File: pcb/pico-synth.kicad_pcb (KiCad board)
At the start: 2 copper layers, 55.8 x 82.8 mm, 49 parts, among them J1 JST XH 2P, J2 JST XH 5P, J3 JST XH 4P, J4 JST XH 3P, SW1 Rotary_Encoder_Switch, U1 Pico, U2 6N137, U3 24LC512, U4 MCP4822, U5 LTC1044, U6 TL071, U7 TL072

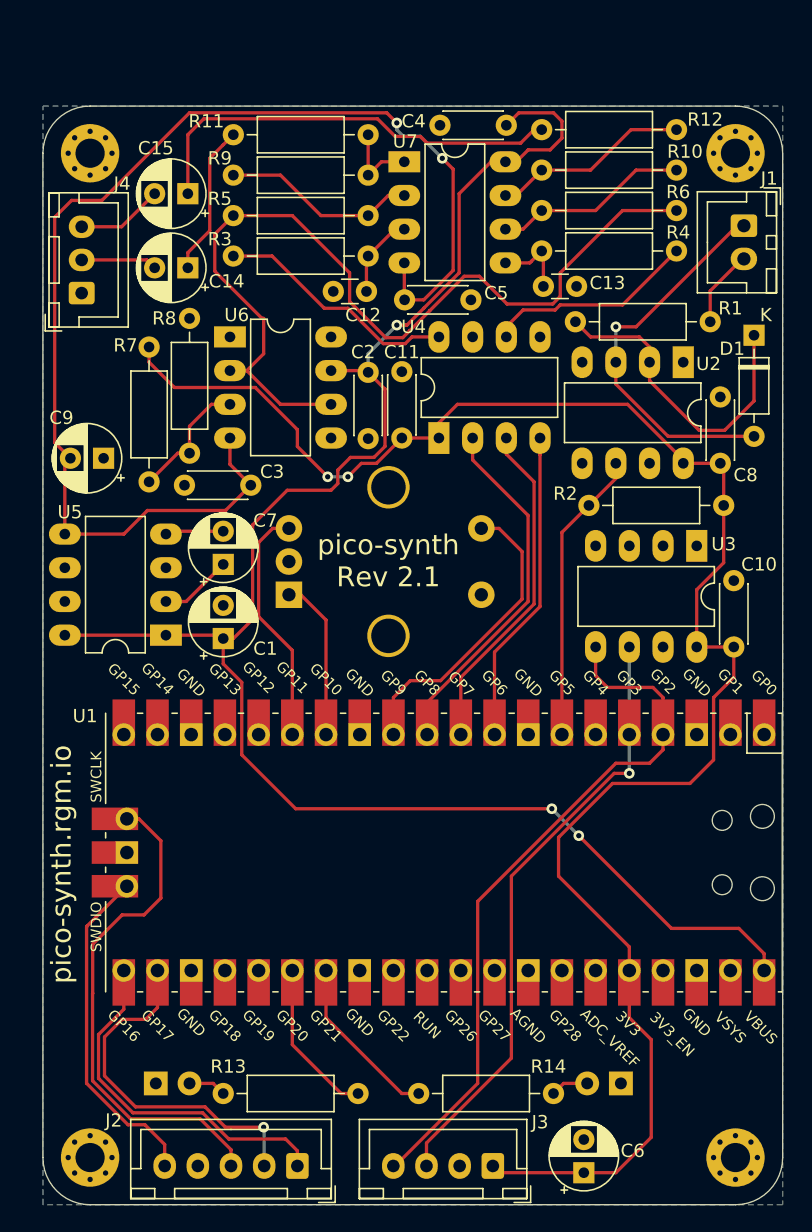
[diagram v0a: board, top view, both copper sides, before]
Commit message: pcb: upgrade to kicad 6
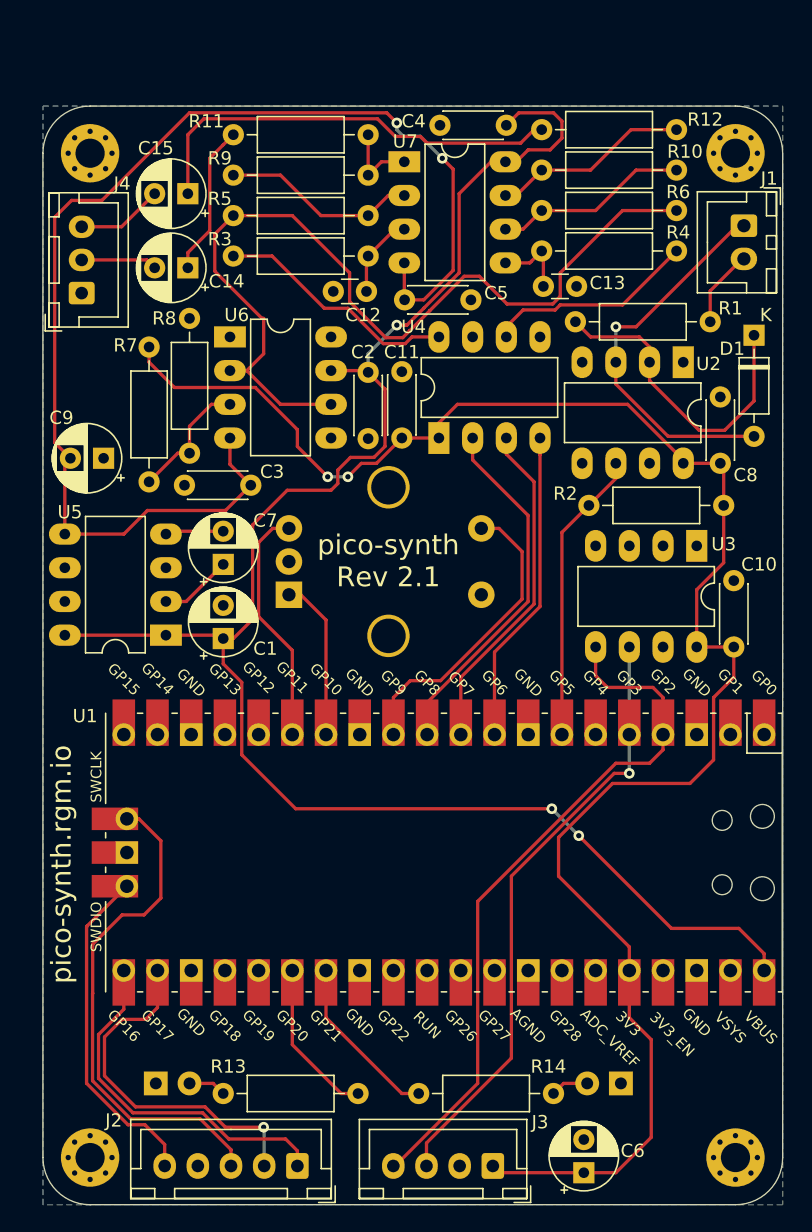
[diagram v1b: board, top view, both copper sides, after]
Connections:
- U1 pad 1: Net-(U1-Pad1) -> unconnected-(U1-Pad1)
- U1 pad 16: Net-(U1-Pad16) -> unconnected-(U1-Pad16)
- U1 pad 17: Net-(U1-Pad17) -> unconnected-(U1-Pad17)
- U1 pad 19: Net-(U1-Pad19) -> unconnected-(U1-Pad19)
- U1 pad 2: Net-(U1-Pad2) -> unconnected-(U1-Pad2)
- U1 pad 20: Net-(U1-Pad20) -> unconnected-(U1-Pad20)
- U1 pad 24: Net-(U1-Pad24) -> unconnected-(U1-Pad24)
- U1 pad 25: Net-(U1-Pad25) -> unconnected-(U1-Pad25)
- U1 pad 29: Net-(U1-Pad29) -> unconnected-(U1-Pad29)
- U1 pad 30: Net-(U1-Pad30) -> unconnected-(U1-Pad30)
- U1 pad 31: Net-(U1-Pad31) -> unconnected-(U1-Pad31)
- U1 pad 32: Net-(U1-Pad32) -> unconnected-(U1-Pad32)
- U1 pad 34: Net-(U1-Pad34) -> unconnected-(U1-Pad34)
- U1 pad 35: Net-(U1-Pad35) -> unconnected-(U1-Pad35)
- U1 pad 37: Net-(U1-Pad37) -> unconnected-(U1-Pad37)
- U1 pad 39: Net-(U1-Pad39) -> unconnected-(U1-Pad39)
- U1 pad 6: Net-(U1-Pad6) -> unconnected-(U1-Pad6)
- U2 pad 1: (no net) -> unconnected-(U2-Pad1)
- U2 pad 7: (no net) -> unconnected-(U2-Pad7)
- U5 pad 6: (no net) -> unconnected-(U5-Pad6)
- U5 pad 7: (no net) -> unconnected-(U5-Pad7)
- U6 pad 1: (no net) -> unconnected-(U6-Pad1)
- U6 pad 5: (no net) -> unconnected-(U6-Pad5)
- U6 pad 8: (no net) -> unconnected-(U6-Pad8)
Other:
- net class Default removed

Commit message: new hardware revision: 3.0
- added better output filter (Sallen-Key low pass filter)
- use MCP4822's LDAC pin to avoid (minimal, negligible :) phase drift
  between the channels
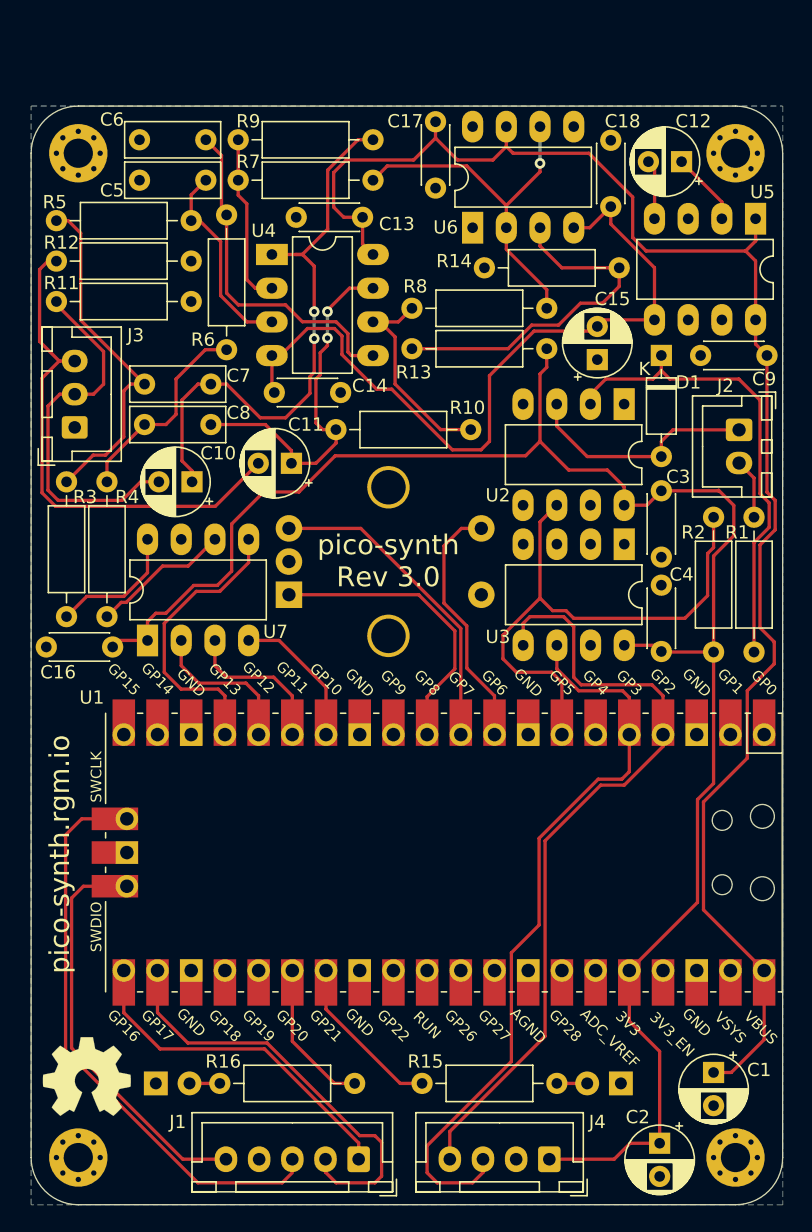
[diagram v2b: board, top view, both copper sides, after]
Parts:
- added C16: 100n, Capacitor_THT:C_Disc_D4.3mm_W1.9mm_P5.00mm, F.Cu at (118.6, 101.6)
- added C17: 100n, Capacitor_THT:C_Disc_D4.3mm_W1.9mm_P5.00mm, F.Cu at (148.0, 62.0)
- added C18: 100n, Capacitor_THT:C_Disc_D4.3mm_W1.9mm_P5.00mm, F.Cu at (161.2, 68.4)
- added R15: 18k, Resistor_THT:R_Axial_DIN0207_L6.3mm_D2.5mm_P10.16mm_Horizontal, F.Cu at (146.9, 134.5)
- added R16: 18k, Resistor_THT:R_Axial_DIN0207_L6.3mm_D2.5mm_P10.16mm_Horizontal, F.Cu at (141.9, 134.5)
- C10, C11, C2: value 100n -> 10u; footprint Capacitor_THT:C_Disc_D4.3mm_W1.9mm_P5.00mm -> Capacitor_THT:CP_Radial_D5.0mm_P2.50mm
- C12: value 4n7 -> 10u; footprint Capacitor_THT:C_Disc_D3.0mm_W1.6mm_P2.50mm -> Capacitor_THT:CP_Radial_D5.0mm_P2.50mm
- C13: value 4n7 -> 100n; footprint Capacitor_THT:C_Disc_D3.0mm_W1.6mm_P2.50mm -> Capacitor_THT:C_Disc_D4.3mm_W1.9mm_P5.00mm
- C14, C9: value 10u -> 100n; footprint Capacitor_THT:CP_Radial_D5.0mm_P2.50mm -> Capacitor_THT:C_Disc_D4.3mm_W1.9mm_P5.00mm
- C5, C8: value 100n -> 4n7; footprint Capacitor_THT:C_Disc_D4.3mm_W1.9mm_P5.00mm -> Capacitor_THT:C_Rect_L7.0mm_W2.5mm_P5.00mm
- C6, C7: value 10u -> 4n7; footprint Capacitor_THT:CP_Radial_D5.0mm_P2.50mm -> Capacitor_THT:C_Rect_L7.0mm_W2.5mm_P5.00mm
- J1: value JST XH 2P -> JST XH 5P; footprint Connector_JST:JST_XH_B2B-XH-A_1x02_P2.50mm_Vertical -> Connector_JST:JST_XH_B5B-XH-A_1x05_P2.50mm_Vertical
- J2: value JST XH 5P -> JST XH 2P; footprint Connector_JST:JST_XH_B5B-XH-A_1x05_P2.50mm_Vertical -> Connector_JST:JST_XH_B2B-XH-A_1x02_P2.50mm_Vertical
- J3: value JST XH 4P -> JST XH 3P; footprint Connector_JST:JST_XH_B4B-XH-A_1x04_P2.50mm_Vertical -> Connector_JST:JST_XH_B3B-XH-A_1x03_P2.50mm_Vertical
- J4: value JST XH 3P -> JST XH 4P; footprint Connector_JST:JST_XH_B3B-XH-A_1x03_P2.50mm_Vertical -> Connector_JST:JST_XH_B4B-XH-A_1x04_P2.50mm_Vertical
- R11, R12: value 1k -> 10k
- R13: value 18k -> 22k
- R14: value 18k -> 10k
- R3, R4: value 470R -> 2k7
- R5, R6: value 56k -> 2k7
- R7: value 22k -> 56k
- R8: value 10k -> 56k
- REF**: moved to F.Cu
- U4: value MCP4822 -> TL072
- U7: value TL072 -> MCP4822
- moved C6 82.9 mm to (130.6, 63.4), turned to 180 degrees
- moved J1 76.1 mm to (142.2, 140.2), turned to 180 degrees
- moved J4 74.2 mm to (156.5, 140.2), turned to 180 degrees
- moved J2 64.7 mm to (170.8, 85.2), turned to -90 degrees
- moved R14 64.0 mm to (161.8, 73.0), turned to 180 degrees
- moved J3 64.0 mm to (120.8, 85.0), turned to 90 degrees
- moved C2 62.1 mm to (164.8, 139.0)
- moved R13 57.9 mm to (156.3, 79.1)
- moved U5 54.4 mm to (172.1, 69.3), turned to -90 degrees
- moved C9 50.6 mm to (172.9, 79.6)
- moved C1 49.3 mm to (168.9, 133.7), turned to -90 degrees
- moved C8 43.5 mm to (126.0, 84.8), turned to 0 degrees
- moved C10 42.7 mm to (129.6, 89.2), turned to 180 degrees
- moved U7 40.9 mm to (126.2, 101.1), turned to 90 degrees
- moved R12 37.9 mm to (119.4, 72.5)
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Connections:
- C10 pad 1: +3V3 -> Net-(C10-Pad1)
- C10 pad 2: GND -> Net-(C10-Pad2)
- C11 pad 1: +3V3 -> Net-(C11-Pad1)
- C11 pad 2: GND -> Net-(C11-Pad2)
- C12 pad 2: GND -> Net-(C12-Pad2)
- C13 pad 1: Net-(C13-Pad1) -> +5V
- C14 pad 1: Net-(C14-Pad1) -> -5V
- C14 pad 2: Net-(C14-Pad2) -> GND
- C15 pad 1: Net-(C15-Pad1) -> GND
- C15 pad 2: Net-(C15-Pad2) -> -5V
- C2 pad 1: +5V -> +3V3
- C3 pad 1: GND -> +3V3
- C3 pad 2: -5V -> GND
- C4 pad 1: +5V -> GND
- C4 pad 2: GND -> +3V3
- C5 pad 1: GND -> Net-(C5-Pad1)
- C5 pad 2: -5V -> GND
- C6 pad 1: +3V3 -> Net-(C6-Pad1)
- C7 pad 2: Net-(C7-Pad2) -> Net-(C10-Pad1)
- C8 pad 1: +3V3 -> Net-(C8-Pad1)
- C8 pad 2: GND -> Net-(C11-Pad1)
- C9 pad 1: GND -> +5V
- C9 pad 2: -5V -> GND
- J1 pad 1: Net-(D1-Pad2) -> DBG_TX
- J1 pad 2: Net-(J1-Pad2) -> DBG_RX
- J2 pad 1: DBG_TX -> Net-(D1-Pad2)
- J2 pad 2: DBG_RX -> Net-(J2-Pad2)
- J3 pad 1: +3V3 -> GND
- J3 pad 2: GND -> Net-(C10-Pad2)
- J3 pad 3: SCL -> Net-(C11-Pad2)
- J4 pad 1: GND -> +3V3
- J4 pad 2: Net-(C14-Pad2) -> GND
- J4 pad 3: Net-(C15-Pad2) -> SCL
- R1 pad 1: Net-(J1-Pad2) -> Net-(J2-Pad2)
- R10 pad 1: Net-(R10-Pad1) -> Net-(C11-Pad1)
- R11 pad 1: Net-(C14-Pad1) -> Net-(C10-Pad2)
- R11 pad 2: Net-(R11-Pad2) -> GND
- R12 pad 1: Net-(C15-Pad1) -> Net-(C11-Pad2)
- R12 pad 2: Net-(R10-Pad1) -> GND
- R13 pad 1: LED2 -> +3V3
- R13 pad 2: Net-(D3-Pad2) -> Net-(R13-Pad2)
- R14 pad 1: LED1 -> Net-(R13-Pad2)
- R14 pad 2: Net-(D2-Pad2) -> GND
- R3 pad 1: Net-(C12-Pad1) -> Net-(C7-Pad1)
- R4 pad 1: Net-(C13-Pad1) -> Net-(C8-Pad1)
- R5 pad 1: VREF -> Net-(C5-Pad1)
- R5 pad 2: Net-(R5-Pad2) -> Net-(C7-Pad1)
- R6 pad 1: VREF -> Net-(C6-Pad1)
- R6 pad 2: Net-(R10-Pad2) -> Net-(C8-Pad1)
- R7 pad 1: +3V3 -> VREF
- R8 pad 1: Net-(R7-Pad2) -> VREF
- R8 pad 2: GND -> Net-(R10-Pad2)
- R9 pad 1: Net-(R11-Pad2) -> Net-(C10-Pad1)
- R9 pad 2: Net-(R5-Pad2) -> Net-(R7-Pad2)
- U1 pad 10: SCK -> ENC_B
- U1 pad 11: CS -> ENC_A
- U1 pad 12: ENC_BT -> unconnected-(U1-Pad12)
- U1 pad 14: ENC_A -> SDI
- U1 pad 15: ENC_B -> SCK
- U1 pad 16: unconnected-(U1-Pad16) -> CS
- U1 pad 17: unconnected-(U1-Pad17) -> LDAC
- U1 pad 9: SDI -> ENC_BT
- U4 pad 1: +3V3 -> Net-(C10-Pad1)
- U4 pad 2: CS -> Net-(R7-Pad2)
- U4 pad 3: SCK -> Net-(C5-Pad1)
- U4 pad 4: SDI -> -5V
- U4 pad 5: GND -> Net-(C6-Pad1)
- U4 pad 6: CH2 -> Net-(R10-Pad2)
- U4 pad 7: GND -> Net-(C11-Pad1)
- U4 pad 8: CH1 -> +5V
- U5 pad 2: Net-(C7-Pad1) -> Net-(C12-Pad1)
- U5 pad 4: Net-(C7-Pad2) -> Net-(C12-Pad2)
- U6 pad 3: Net-(R7-Pad2) -> Net-(R13-Pad2)
- U7 pad 1: Net-(R11-Pad2) -> +3V3
- U7 pad 2: Net-(R5-Pad2) -> CS
- U7 pad 3: Net-(C12-Pad1) -> SCK
- U7 pad 4: -5V -> SDI
- U7 pad 5: Net-(C13-Pad1) -> LDAC
- U7 pad 6: Net-(R10-Pad2) -> CH2
- U7 pad 7: Net-(R10-Pad1) -> GND
- U7 pad 8: +5V -> CH1
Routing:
- net Net-(C10-Pad1): track 0.00 -> 43.7 mm, vias 0 -> 2
- net VREF: track 68.3 -> 27.7 mm, vias 0 -> 1
- net Net-(C11-Pad2): track 0.00 -> 38.7 mm
- net -5V: track 94.6 -> 57.5 mm, vias 2 -> 0
- net Net-(C15-Pad1): track 32.8 -> 0.00 mm
- net Net-(C10-Pad2): track 0.00 -> 28.2 mm
- net Net-(C11-Pad1): track 0.00 -> 27.6 mm, vias 0 -> 2
- net Net-(R13-Pad2): track 0.00 -> 27.0 mm
- net Net-(C6-Pad1): track 0.00 -> 26.0 mm
- net LDAC: track 0.00 -> 21.9 mm
- net Net-(C7-Pad1): track 5.48 -> 26.6 mm
- net MIDI_RX: track 22.1 -> 42.4 mm
- net CS: track 27.2 -> 11.6 mm
- net Net-(C8-Pad1): track 0.00 -> 15.2 mm
- net Net-(C5-Pad1): track 0.00 -> 15.1 mm
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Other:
- board size 55.8 x 82.8 mm -> 56.6 x 82.8 mm
- board text added: "pico-synth Rev 3.0"
- board text removed: "pico-synth Rev 2.1"

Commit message: pcb: new hardware revision: 4.0
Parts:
- removed C13, C14, C16, C17, C18: 100n, Capacitor_THT:C_Disc_D4.3mm_W1.9mm_P5.00mm
- removed C15: 10u, Capacitor_THT:CP_Radial_D5.0mm_P2.50mm
- removed the J3 at (120.8, 85.0)
- removed the R13 at (156.3, 79.1)
- removed the R14 at (161.8, 73.0)
- removed U6: TL071, Package_DIP:DIP-8_W7.62mm_LongPads
- removed U7: MCP4822, Package_DIP:DIP-8_W7.62mm_LongPads
- added J4: JST XH 3P, Connector_JST:JST_XH_B3B-XH-A_1x03_P2.50mm_Vertical, F.Cu at (120.9, 84.5)
- C11, C12: value 10u -> 100n; footprint Capacitor_THT:CP_Radial_D5.0mm_P2.50mm -> Capacitor_THT:C_Disc_D4.3mm_W1.9mm_P5.00mm
- C9: value 100n -> 10u; footprint Capacitor_THT:C_Disc_D4.3mm_W1.9mm_P5.00mm -> Capacitor_THT:CP_Radial_D5.0mm_P2.50mm
- R10, R9: value 39k -> 33k
- R3, R4, R5, R6: value 2k7 -> 2k2
- U4: value TL072 -> TLV272
- U5: value LTC1044 -> MCP4822
- moved C12 60.0 mm to (118.6, 101.2), turned to 0 degrees
- moved U5 55.7 mm to (126.2, 101.0), turned to 90 degrees
- moved C9 45.5 mm to (127.5, 77.2), turned to 90 degrees
- moved R9 25.0 mm to (166.9, 71.5)
- moved R6 23.9 mm to (149.2, 85.9), turned to 180 degrees
- moved R5 23.8 mm to (149.2, 82.8)
- moved R7 17.4 mm to (126.6, 71.6), turned to 0 degrees
- moved R12 16.1 mm to (119.5, 88.6), turned to -90 degrees
- moved R3 15.9 mm to (136.0, 89.9), turned to 180 degrees
- moved C11 15.8 mm to (149.9, 78.5), turned to 90 degrees
- moved C6 15.5 mm to (136.6, 77.7)
- moved R10 14.2 mm to (152.4, 77.6)
- moved R11 13.5 mm to (122.6, 88.6), turned to -90 degrees
- moved R4 13.0 mm to (136.0, 86.9), turned to 180 degrees
- moved U4 11.4 mm to (147.1, 72.1), turned to -90 degrees
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- renumbered J4 to J3, R15 to R13, R16 to R14
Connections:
- C11 pad 1: Net-(C11-Pad1) -> +5V
- C11 pad 2: Net-(C11-Pad2) -> GND
- C12 pad 1: Net-(C12-Pad1) -> GND
- C12 pad 2: Net-(C12-Pad2) -> +3V3
- C7 pad 2: Net-(C10-Pad1) -> Net-(C7-Pad2)
- C8 pad 2: Net-(C11-Pad1) -> Net-(C10-Pad1)
- C9 pad 1: +5V -> Net-(C7-Pad2)
- C9 pad 2: GND -> Net-(C9-Pad2)
- R10 pad 1: Net-(C11-Pad1) -> Net-(C10-Pad1)
- R11 pad 1: Net-(C10-Pad2) -> Net-(C9-Pad2)
- R12 pad 1: Net-(C11-Pad2) -> Net-(C10-Pad2)
- R7 pad 1: VREF -> GND
- R8 pad 1: VREF -> GND
- R9 pad 1: Net-(C10-Pad1) -> Net-(C7-Pad2)
- U4 pad 1: Net-(C10-Pad1) -> Net-(C7-Pad2)
- U4 pad 4: -5V -> GND
- U4 pad 7: Net-(C11-Pad1) -> Net-(C10-Pad1)
- U5 pad 1: +5V -> +3V3
- U5 pad 2: Net-(C12-Pad1) -> CS
- U5 pad 3: GND -> SCK
- U5 pad 4: Net-(C12-Pad2) -> SDI
- U5 pad 5: -5V -> LDAC
- U5 pad 6: unconnected-(U5-Pad6) -> CH2
- U5 pad 7: unconnected-(U5-Pad7) -> GND
- U5 pad 8: +5V -> CH1
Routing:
- net -5V: track 57.5 -> 0.00 mm
- net Net-(C7-Pad2): track 0.00 -> 53.2 mm
- net Net-(C11-Pad2): track 38.7 -> 0.00 mm
- net +5V: track 122.2 -> 91.6 mm
- net VREF: track 27.7 -> 0.00 mm, vias 1 -> 0
- net Net-(C11-Pad1): track 27.6 -> 0.00 mm, vias 2 -> 0
- net Net-(R13-Pad2): track 27.0 -> 0.00 mm
- net Net-(C9-Pad2): track 0.00 -> 18.5 mm
- net Net-(R7-Pad2): track 13.0 -> 26.4 mm
- net Net-(C5-Pad1): track 15.1 -> 26.6 mm
- net Net-(C7-Pad1): track 26.6 -> 15.4 mm
- net DBG_RX: track 32.4 -> 21.3 mm
- net Net-(J2-Pad2): track 4.55 -> 15.0 mm
- net Net-(D1-Pad1): track 36.1 -> 26.1 mm
- net Net-(C6-Pad1): track 26.0 -> 16.6 mm
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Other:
- board size 56.6 x 82.8 mm -> 56.6 x 74.5 mm
- board text added: "pico-synth Rev 4.0"
- board text removed: "pico-synth Rev 3.0"
